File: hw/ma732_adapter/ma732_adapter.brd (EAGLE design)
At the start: 5.9 x 6 mm, 15 parts

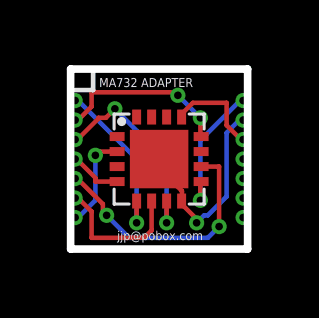
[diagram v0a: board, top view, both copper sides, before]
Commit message: Tweak to get minimum size up to oshpark standards
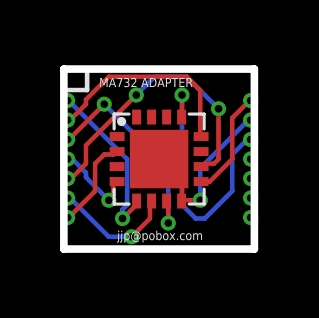
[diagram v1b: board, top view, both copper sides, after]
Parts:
- moved A 0.25 mm to (-3.05, -1.95)
- moved B 0.25 mm to (-3.05, -1.30)
- moved CLK 0.25 mm to (-3.05, 1.30)
- moved CSN 0.25 mm to (-3.05, 1.95)
- moved GND 0.25 mm to (3.05, 1.30)
- moved MISO 0.25 mm to (-3.05, 0.65)
- moved MOSI 0.25 mm to (-3.05, 0.00)
- moved PWM 0.25 mm to (3.05, 1.95)
- moved TEST 0.25 mm to (-3.05, -0.65)
- moved U 0.25 mm to (3.05, -0.65)
- moved V 0.25 mm to (3.05, -1.30)
- moved VDD 0.25 mm to (3.05, 0.00)
- moved VDD3V 0.25 mm to (3.05, 0.65)
- moved W 0.25 mm to (3.05, -1.95)
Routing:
- net N$24: track 3.27 -> 8.83 mm, vias 0 -> 1
- net N$19: track 8.54 -> 9.75 mm
- net N$23: track 6.93 -> 5.78 mm
- net N$16: track 5.88 -> 6.97 mm, vias 2 -> 0
- net N$22: track 4.67 -> 3.62 mm, vias 1 -> 0
- net N$18: track 1.78 -> 2.83 mm, vias 0 -> 1
- net N$20: track 4.73 -> 4.24 mm, vias 0 -> 1
- net N$21: track 3.30 -> 3.13 mm, vias 1 -> 0
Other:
- board size 5.9 x 6 mm -> 6.3 x 6 mm

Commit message: More size tweaks
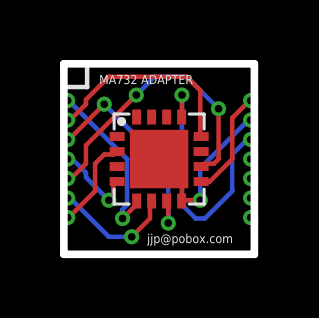
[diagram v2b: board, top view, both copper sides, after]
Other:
- board size 6.3 x 6 mm -> 6.3 x 6.3 mm
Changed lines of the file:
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@@
 <board>
 <plain>
-<wire x1="-3.175" y1="3" x2="3.175" y2="3" width="0.254" layer="20"/>
-<wire x1="3.175" y1="3" x2="3.175" y2="-3" width="0.254" layer="20"/>
-<wire x1="3.175" y1="-3" x2="-3.175" y2="-3" width="0.254" layer="20"/>
-<wire x1="-3.175" y1="-3" x2="-3.175" y2="3" width="0.254" layer="20"/>
-<text x="-2" y="2.4" size="0.3" layer="21">MA732 ADAPTER</text>
-<text x="-1.4" y="-2.7" size="0.3" layer="21">jjp@pobox.com</text>
-<wire x1="-3.1" y1="2.3" x2="-2.4" y2="2.3" width="0.1524" layer="21"/>
-<wire x1="-2.4" y1="2.3" x2="-2.4" y2="2.9" width="0.1524" layer="21"/>
+<wire x1="-3.175" y1="3.175" x2="3.175" y2="3.175" width="0.254" layer="20"/>
+<wire x1="3.175" y1="3.175" x2="3.175" y2="-3.175" width="0.254" layer="20"/>
+<wire x1="3.175" y1="-3.175" x2="-3.175" y2="-3.175" width="0.254" layer="20"/>
+<wire x1="-3.175" y1="-3.175" x2="-3.175" y2="3.175" width="0.254" layer="20"/>
+<text x="-2" y="2.5" size="0.3" layer="21">MA732 ADAPTER</text>
+<text x="-0.4" y="-2.8" size="0.3" layer="21">jjp@pobox.com</text>
+<wire x1="-3.1" y1="2.4" x2="-2.4" y2="2.4" width="0.1524" layer="21"/>
+<wire x1="-2.4" y1="2.4" x2="-2.4" y2="3.1" width="0.1524" layer="21"/>
 </plain>
 <attributes>
